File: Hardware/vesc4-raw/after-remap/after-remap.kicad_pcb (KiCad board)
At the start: 4 copper layers, 38.5 x 65 mm, 127 parts, among them K1 SERVO, P1 HALL/Encoder, P101 CANBUS, P2 SWD, P3 PWR_COMM, P4 IN+, P5 IN-, P6 MOTOR1, P7 MOTOR2, P9 MOTOR3, Q1 IPT007N06NATMA1, Q2 IPT007N06NATMA1, Q3 IPT007N06NATMA1, Q4 IPT007N06NATMA1, Q5 IPT007N06NATMA1, Q6 IPT007N06NATMA1, U1 STM32F40X_LQFP64, U2 TC2117, U3 DRV8302, U401 SN65HVD232, X1 MINI-USB-SHIELD-32005-201, X2 8MHz 10ppm

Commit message: changed phase 3
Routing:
- net /Power MOSFETS/Q5-s_Q6-d: track 166.9 -> 175.3 mm, vias 18 -> 20
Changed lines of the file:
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@@
-	)
-	(segment
-		(start 86.36 90.932)
-		(end 84.836 90.678)
-		(width 0.508)
-		(layer "F.Cu")
-		(net 69)
 	)
 	(segment
@@
 	)
 	(segment
+		(start 86.36 90.932)
+		(end 86.4742 90.932)
+		(width 1.27)
+		(layer "F.Cu")
+		(net 69)
+	)
+	(segment
 		(start 86.36 89.154)
 		(end 86.36 87.122)
@@
 		(end 85.725 87.24646)
 		(width 0.508)
+		(layer "F.Cu")
+		(net 69)
+	)
+	(segment
+		(start 87.7 90.7)
+		(end 87.468 90.932)
+		(width 1.27)
 		(layer "F.Cu")
 		(net 69)
@@
 	)
 	(segment
+		(start 85.8 90.932)
+		(end 84.582 90.932)
+		(width 1.27)
+		(layer "F.Cu")
+		(net 69)
+	)
+	(segment
+		(start 87.468 90.932)
+		(end 85.8 90.932)
+		(width 1.27)
+		(layer "F.Cu")
+		(net 69)
+	)
+	(segment
+		(start 87.9062 89.5)
+		(end 86.948527 88.542327)
+		(width 0.2032)
+		(layer "F.Cu")
+		(net 69)
+	)
+	(segment
+		(start 85.8 90.932)
+		(end 86.4742 90.932)
+		(width 1.27)
+		(layer "F.Cu")
+		(net 69)
+	)
+	(segment
+		(start 86.749702 88.542327)
+		(end 87.8441 89.636725)
+		(width 1.27)
+		(layer "F.Cu")
+		(net 69)
+	)
+	(segment
 		(start 104.267 104.233266)
 		(end 104.267 107.442)
@@
 	)
 	(segment
-		(start 86.36 90.932)
-		(end 84.582 90.932)
+		(start 86.749702 90.656498)
+		(end 86.749702 88.542327)
 		(width 1.27)
 		(layer "F.Cu")
@@
 	)
 	(segment
+		(start 86.749702 88.542327)
+		(end 87.8441 88.542327)
+		(width 1.27)
+		(layer "F.Cu")
+		(net 69)
+	)
+	(segment
+		(start 87.8441 89.636725)
+		(end 87.8441 90.442327)
+		(width 1.27)
+		(layer "F.Cu")
+		(net 69)
+	)
+	(segment
 		(start 85.979 87.24646)
 		(end 85.979 83.693)
@@
 	)
 	(segment
+		(start 86.948527 88.542327)
+		(end 86.749702 88.542327)
+		(width 0.2032)
+		(layer "F.Cu")
+		(net 69)
+	)
+	(segment
 		(start 105.15854 110.779958)
 		(end 104.14 109.761418)
@@
 		(net 69)
 	)
-	(via
-		(at 86.36 87.122)
-		(size 1.524)
-		(drill 0.762)
-		(layers "F.Cu" "B.Cu")
-		(net 69)
-	)
-	(via
-		(at 84.582 89.154)
-		(size 1.524)
-		(drill 0.762)
+	(segment
+		(start 86.4742 90.932)
+		(end 86.749702 90.656498)
+		(width 1.27)
+		(layer "F.Cu")
+		(net 69)
+	)
+	(via
+		(at 86.749702 88.542327)
+		(size 0.8)
+		(drill 0.5)
+		(layers "F.Cu" "B.Cu")
+		(net 69)
+	)
+	(via
+		(at 87.949702 88.542327)
+		(size 0.8)
+		(drill 0.5)
+		(layers "F.Cu" "B.Cu")
+		(net 69)
+	)
+	(via
+		(at 84.349702 90.442327)
+		(size 0.8)
+		(drill 0.5)
+		(layers "F.Cu" "B.Cu")
+		(net 69)
+	)
+	(via
+		(at 84.349702 88.542327)
+		(size 0.8)
+		(drill 0.5)
 		(layers "F.Cu" "B.Cu")
 		(net 69)
@@
 	)
 	(via
-		(at 82.804 90.932)
-		(size 1.524)
-		(drill 0.762)
-		(layers "F.Cu" "B.Cu")
-		(net 69)
-	)
-	(via
-		(at 82.804 87.122)
-		(size 1.524)
-		(drill 0.762)
-		(layers "F.Cu" "B.Cu")
-		(net 69)
-	)
-	(via
-		(at 82.804 89.154)
-		(size 1.524)
-		(drill 0.762)
-		(layers "F.Cu" "B.Cu")
-		(net 69)
-	)
-	(via
-		(at 81.026 89.154)
-		(size 1.524)
-		(drill 0.762)
+		(at 81.949702 88.542327)
+		(size 0.8)
+		(drill 0.5)
 		(layers "F.Cu" "B.Cu")
 		(net 69)
@@
 		(at 91.44 86.868)
 		(size 0.889)
+		(drill 0.5)
+		(layers "F.Cu" "B.Cu")
+		(net 69)
+	)
+	(via
+		(at 83.149702 88.542327)
+		(size 0.8)
+		(drill 0.5)
+		(layers "F.Cu" "B.Cu")
+		(net 69)
+	)
+	(via
+		(at 85.549702 88.542327)
+		(size 0.8)
 		(drill 0.5)
 		(layers "F.Cu" "B.Cu")
@@
 	)
 	(via
+		(at 80.749702 90.442327)
+		(size 0.8)
+		(drill 0.5)
+		(layers "F.Cu" "B.Cu")
+		(net 69)
+	)
+	(via
 		(at 104.5 104.000266)
 		(size 0.8)
 		(drill 0.5)
-		(layers "F.Cu" "B.Cu")
-		(net 69)
-	)
-	(via
-		(at 81.026 90.932)
-		(size 1.524)
-		(drill 0.762)
 		(layers "F.Cu" "B.Cu")
 		(net 69)
@@
 	)
 	(via
-		(at 86.36 90.932)
-		(size 1.524)
-		(drill 0.762)
+		(at 81.949702 90.442327)
+		(size 0.8)
+		(drill 0.5)
 		(layers "F.Cu" "B.Cu")
 		(net 69)
@@
 	)
 	(via
-		(at 84.582 87.122)
-		(size 1.524)
-		(drill 0.762)
-		(layers "F.Cu" "B.Cu")
-		(net 69)
-	)
-	(via
-		(at 81.026 87.122)
-		(size 1.524)
-		(drill 0.762)
-		(layers "F.Cu" "B.Cu")
-		(net 69)
-	)
-	(via
-		(at 86.36 89.154)
-		(size 1.524)
-		(drill 0.762)
-		(layers "F.Cu" "B.Cu")
-		(net 69)
-	)
-	(via
-		(at 84.582 90.932)
-		(size 1.524)
-		(drill 0.762)
+		(at 87.949702 90.442327)
+		(size 0.8)
+		(drill 0.5)
+		(layers "F.Cu" "B.Cu")
+		(net 69)
+	)
+	(via
+		(at 86.749702 90.442327)
+		(size 0.8)
+		(drill 0.5)
+		(layers "F.Cu" "B.Cu")
+		(net 69)
+	)
+	(via
+		(at 83.149702 90.442327)
+		(size 0.8)
+		(drill 0.5)
+		(layers "F.Cu" "B.Cu")
+		(net 69)
+	)
+	(via
+		(at 85.549702 90.442327)
+		(size 0.8)
+		(drill 0.5)
+		(layers "F.Cu" "B.Cu")
+		(net 69)
+	)
+	(via
+		(at 80.749702 88.542327)
+		(size 0.8)
+		(drill 0.5)
 		(layers "F.Cu" "B.Cu")
 		(net 69)
@@
 	)
 	(segment
-		(start 86.614 86.868)
-		(end 86.36 87.122)
-		(width 1.27)
-		(layer "In2.Cu")
-		(net 69)
-	)
-	(segment
 		(start 98.539266 104.000266)
 		(end 95.504 100.965)
@@
 	)
 	(segment
+		(start 88.424029 86.868)
+		(end 86.749702 88.542327)
+		(width 1.27)
+		(layer "In2.Cu")
+		(net 69)
+	)
+	(segment
 		(start 89.789 111.76)
 		(end 93.726 111.76)
@@
 	)
 	(segment
-		(start 91.44 86.868)
-		(end 86.614 86.868)
-		(width 1.27)
-		(layer "In2.Cu")
-		(net 69)
-	)
-	(segment
 		(start 90.932 100.965)
 		(end 88.392 103.505)
@@
 		(layer "In2.Cu")
 		(net 69)
+	)
+	(segment
+		(start 91.44 86.868)
+		(end 88.424029 86.868)
+		(width 1.27)
+		(layer "In2.Cu")
+		(net 69)

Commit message: change phase tengah
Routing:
- net /Power MOSFETS/Q3-s_Q4-d: track 145.0 -> 145.9 mm, vias 17 -> 19

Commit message: pindahin via untuk perbanyak contact
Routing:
- net /Power MOSFETS/Q3-s_Q4-d: track 145.9 -> 153.3 mm
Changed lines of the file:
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@@
 	(segment
 		(start 104.394 91.694)
-		(end 105.537509 92.837509)
+		(end 104.4 91.7)
 		(width 0.635)
 		(layer "In1.Cu")
@@
 	)
 	(segment
-		(start 105.537509 92.837509)
-		(end 105.537509 101.941532)
+		(start 104.4 93.4)
+		(end 105.537509 94.537509)
 		(width 0.635)
 		(layer "In1.Cu")
@@
 	)
 	(segment
-		(start 105.537509 101.941532)
+		(start 105.537509 94.537509)
 		(end 105.537509 102.507217)
 		(width 0.635)
@@
 	)
 	(segment
+		(start 104.4 91.7)
+		(end 104.4 93.4)
+		(width 0.635)
+		(layer "In1.Cu")
+		(net 17)
+	)
+	(segment
 		(start 102.9966 112.845202)
 		(end 102.596601 113.245201)
@@
 	)
 	(segment
-		(start 100.7441 88.68528)
-		(end 100.7441 90.58528)
+		(start 100.7441 90.58528)
+		(end 100.65138 90.678)
 		(width 1.27)
 		(layer "F.Cu")
@@
 	)
 	(segment
-		(start 99.0186 88.9)
-		(end 100.52938 88.9)
-		(width 1.27)
-		(layer "F.Cu")
-		(net 68)
-	)
-	(segment
 		(start 97.79 82.804)
 		(end 98.171 82.804)
@@
 	)
 	(segment
+		(start 100.52938 88.9)
+		(end 100.7441 88.68528)
+		(width 1.27)
+		(layer "F.Cu")
+		(net 68)
+	)
+	(segment
 		(start 102.489 108.839)
 		(end 102.489 105.41)
@@
 	)
 	(segment
-		(start 100.7441 90.58528)
-		(end 100.65138 90.678)
+		(start 98.4186 89.5)
+		(end 99.0186 88.9)
 		(width 1.27)
 		(layer "F.Cu")
@@
 	)
 	(segment
-		(start 100.52938 88.9)
-		(end 100.7441 88.68528)
+		(start 100.65138 90.678)
+		(end 100.32938 91)
 		(width 1.27)
 		(layer "F.Cu")
@@
 	)
 	(segment
+		(start 100.7441 88.68528)
+		(end 100.7441 90.58528)
+		(width 1.27)
+		(layer "F.Cu")
+		(net 68)
+	)
+	(segment
 		(start 102.489 104.5337)
 		(end 103.790707 103.231993)
@@
 	)
 	(segment
+		(start 100.32938 91)
+		(end 93.732 91)
+		(width 1.27)
+		(layer "F.Cu")
+		(net 68)
+	)
+	(segment
 		(start 95.758 90.678)
 		(end 97.79 90.678)
@@
 	)
 	(segment
-		(start 98.4186 89.5)
-		(end 99.0186 88.9)
-		(width 1.27)
-		(layer "F.Cu")
-		(net 68)
-	)
-	(segment
 		(start 95.758 90.678)
 		(end 95.758 88.9)
@@
 	)
 	(segment
+		(start 99.0186 88.9)
+		(end 100.52938 88.9)
+		(width 1.27)
+		(layer "F.Cu")
+		(net 68)
+	)
+	(segment
 		(start 102.730299 110.730027)
 		(end 102.730299 109.080299)
@@
 	)
 	(via
-		(at 96.033048 90.496332)
+		(at 96.033048 91.234337)
 		(size 0.8)
 		(drill 0.5)
@@
 	)
 	(via
-		(at 100.833048 88.596332)
+		(at 100.833048 87.72272)
 		(size 0.8)
 		(drill 0.5)
@@
 	)
 	(via
-		(at 96.033048 88.596332)
+		(at 96.033048 87.72272)
 		(size 0.8)
 		(drill 0.5)
@@
 	)
 	(via
-		(at 93.633048 88.596332)
+		(at 93.633048 87.72272)
 		(size 0.8)
 		(drill 0.5)
@@
 	)
 	(via
-		(at 94.833048 90.496332)
+		(at 94.833048 91.234337)
 		(size 0.8)
 		(drill 0.5)
@@
 	)
 	(via
-		(at 98.433048 90.496332)
+		(at 98.433048 91.234337)
 		(size 0.8)
 		(drill 0.5)
@@
 	)
 	(via
-		(at 99.633048 90.496332)
+		(at 99.633048 91.234337)
 		(size 0.8)
 		(drill 0.5)
@@
 	)
 	(via
-		(at 93.633048 90.496332)
+		(at 93.633048 91.234337)
 		(size 0.8)
 		(drill 0.5)
@@
 	)
 	(via
-		(at 94.833048 88.596332)
+		(at 94.833048 87.72272)
 		(size 0.8)
 		(drill 0.5)
@@
 	)
 	(via
-		(at 97.233048 88.596332)
+		(at 97.233048 87.72272)
 		(size 0.8)
 		(drill 0.5)
@@
 	)
 	(via
-		(at 97.233048 90.496332)
+		(at 97.233048 91.234337)
 		(size 0.8)
 		(drill 0.5)
@@
 	)
 	(via
-		(at 98.433048 88.596332)
+		(at 98.433048 87.72272)
 		(size 0.8)
 		(drill 0.5)
@@
 	)
 	(via
-		(at 99.633048 88.596332)
+		(at 99.633048 87.72272)
 		(size 0.8)
 		(drill 0.5)
@@
 	)
 	(via
-		(at 100.833048 90.496332)
+		(at 100.833048 91.234337)
 		(size 0.8)
 		(drill 0.5)
@@
 	)
 	(segment
+		(start 102.010328 88.9)
+		(end 103.378 88.9)
+		(width 0.635)
+		(layer "In1.Cu")
+		(net 68)
+	)
+	(segment
 		(start 97.396311 111.391689)
 		(end 104.406689 111.391689)
@@
 	)
 	(segment
+		(start 107.1 102.691825)
+		(end 106.159825 103.632)
+		(width 0.635)
+		(layer "In1.Cu")
+		(net 68)
+	)
+	(segment
 		(start 104.406689 111.391689)
 		(end 106.172 113.157)
@@
 	)
 	(segment
-		(start 103.378 88.9)
-		(end 107.1 92.622)
-		(width 0.635)
+		(start 105.994139 104.031999)
+		(end 105.59414 103.632)
+		(width 0.254)
 		(layer "In1.Cu")
 		(net 68)
 	)
 	(segment
-		(start 107.1 102.691825)
-		(end 106.159825 103.632)
-		(width 0.635)
+		(start 91.2 123.6)
+		(end 90.800001 123.200001)
+		(width 0.254)
 		(layer "In1.Cu")
 		(net 68)
 	)
 	(segment
-		(start 105.994139 104.031999)
-		(end 105.59414 103.632)
-		(width 0.254)
+		(start 105.5 93.1)
+		(end 107.1 94.7)
+		(width 0.635)
 		(layer "In1.Cu")
 		(net 68)
 	)
 	(segment
-		(start 91.2 123.6)
-		(end 90.800001 123.200001)
-		(width 0.254)
+		(start 99.633048 87.72272)
+		(end 100.833048 87.72272)
+		(width 0.635)
 		(layer "In1.Cu")
 		(net 68)
@@
 	)
 	(segment
-		(start 99.633048 88.596332)
-		(end 99.936716 88.9)
-		(width 0.635)
-		(layer "In1.Cu")
-		(net 68)
-	)
-	(segment
 		(start 106.159825 103.632)
 		(end 105.41 103.632)
@@
 	)
 	(segment
-		(start 107.1 92.622)
-		(end 107.1 102.691825)
+		(start 100.833048 87.72272)
+		(end 102.010328 88.9)
 		(width 0.635)
 		(layer "In1.Cu")
@@
 	)
 	(segment
-		(start 99.936716 88.9)
-		(end 103.378 88.9)
+		(start 105.5 91.022)
+		(end 105.5 93.1)
 		(width 0.635)
 		(layer "In1.Cu")
@@
 	)
 	(segment
+		(start 107.1 94.7)
+		(end 107.1 102.691825)
+		(width 0.635)
+		(layer "In1.Cu")
+		(net 68)
+	)
+	(segment
+		(start 103.378 88.9)
+		(end 105.5 91.022)
+		(width 0.635)
+		(layer "In1.Cu")
+		(net 68)
+	)
+	(segment
 		(start 83.312 85.598)
 		(end 83.312 87.122)
@@
 	)
 	(via
-		(at 86.749702 88.542327)
+		(at 86.730095 87.72272)
 		(size 0.8)
 		(drill 0.5)
@@
 	)
 	(via
-		(at 87.949702 88.542327)
+		(at 87.930095 87.72272)
 		(size 0.8)
 		(drill 0.5)
@@
 	)
 	(via
-		(at 84.349702 90.442327)
+		(at 84.341138 91.234337)
 		(size 0.8)
 		(drill 0.5)
@@
 	)
 	(via
-		(at 84.349702 88.542327)
+		(at 84.330095 87.72272)
 		(size 0.8)
 		(drill 0.5)
@@
 	)
 	(via
-		(at 81.949702 88.542327)
+		(at 81.930095 87.72272)
 		(size 0.8)
 		(drill 0.5)
@@
 	)
 	(via
-		(at 83.149702 88.542327)
+		(at 83.130095 87.72272)
 		(size 0.8)
 		(drill 0.5)
@@
 	)
 	(via
-		(at 85.549702 88.542327)
+		(at 85.530095 87.72272)
 		(size 0.8)
 		(drill 0.5)
@@
 	)
 	(via
-		(at 80.749702 90.442327)
+		(at 80.741138 91.234337)
 		(size 0.8)
 		(drill 0.5)
@@
 	)
 	(via
-		(at 81.949702 90.442327)
+		(at 81.941138 91.234337)
 		(size 0.8)
 		(drill 0.5)
@@
 	)
 	(via
-		(at 87.949702 90.442327)
+		(at 87.941138 91.234337)
 		(size 0.8)
 		(drill 0.5)
@@
 	)
 	(via
-		(at 86.749702 90.442327)
+		(at 86.741138 91.234337)
 		(size 0.8)
 		(drill 0.5)
@@
 	)
 	(via
-		(at 83.149702 90.442327)
+		(at 83.141138 91.234337)
 		(size 0.8)
 		(drill 0.5)
@@
 	)
 	(via
-		(at 85.549702 90.442327)
+		(at 85.541138 91.234337)
 		(size 0.8)
 		(drill 0.5)
@@
 	)
 	(via
-		(at 80.749702 88.542327)
+		(at 80.730095 87.72272)
 		(size 0.8)
 		(drill 0.5)

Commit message: done changed via numpuk
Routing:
- net /Power MOSFETS/Q1-s_Q2-d: track 150.9 -> 159.1 mm, vias 17 -> 19

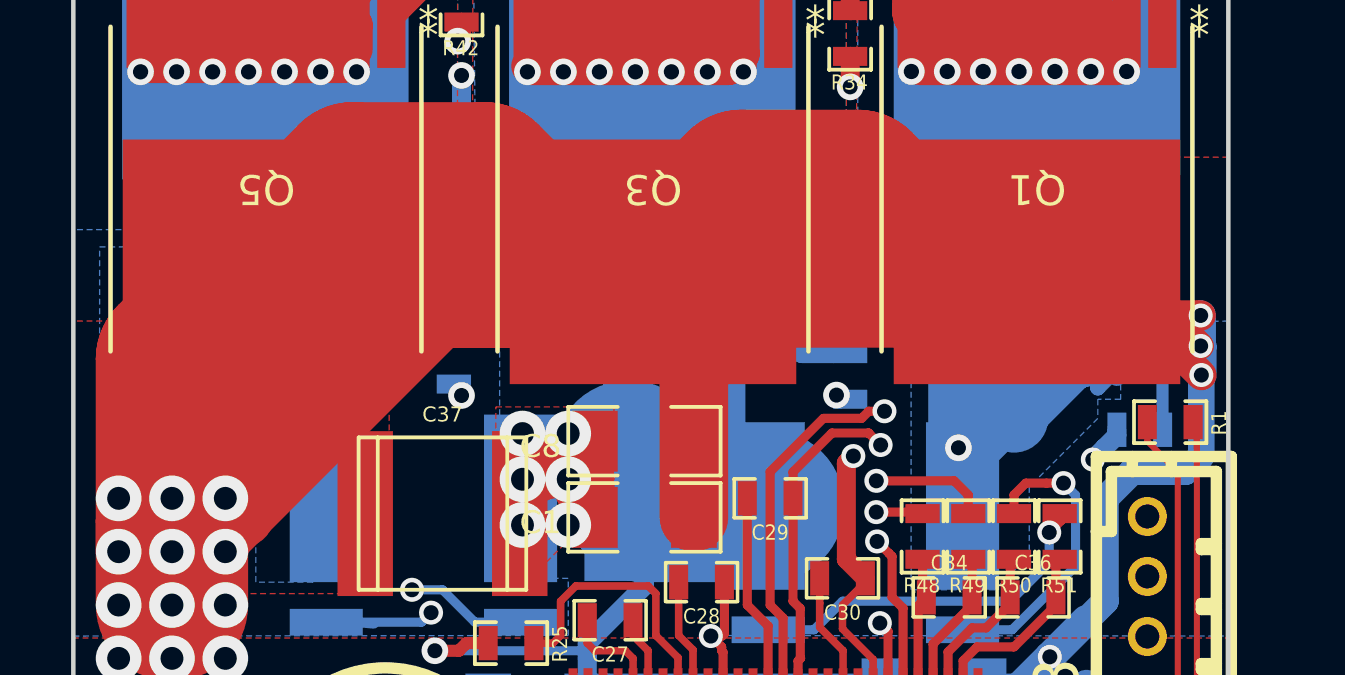
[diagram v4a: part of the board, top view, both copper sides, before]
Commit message: added thermal vias on front mosfets
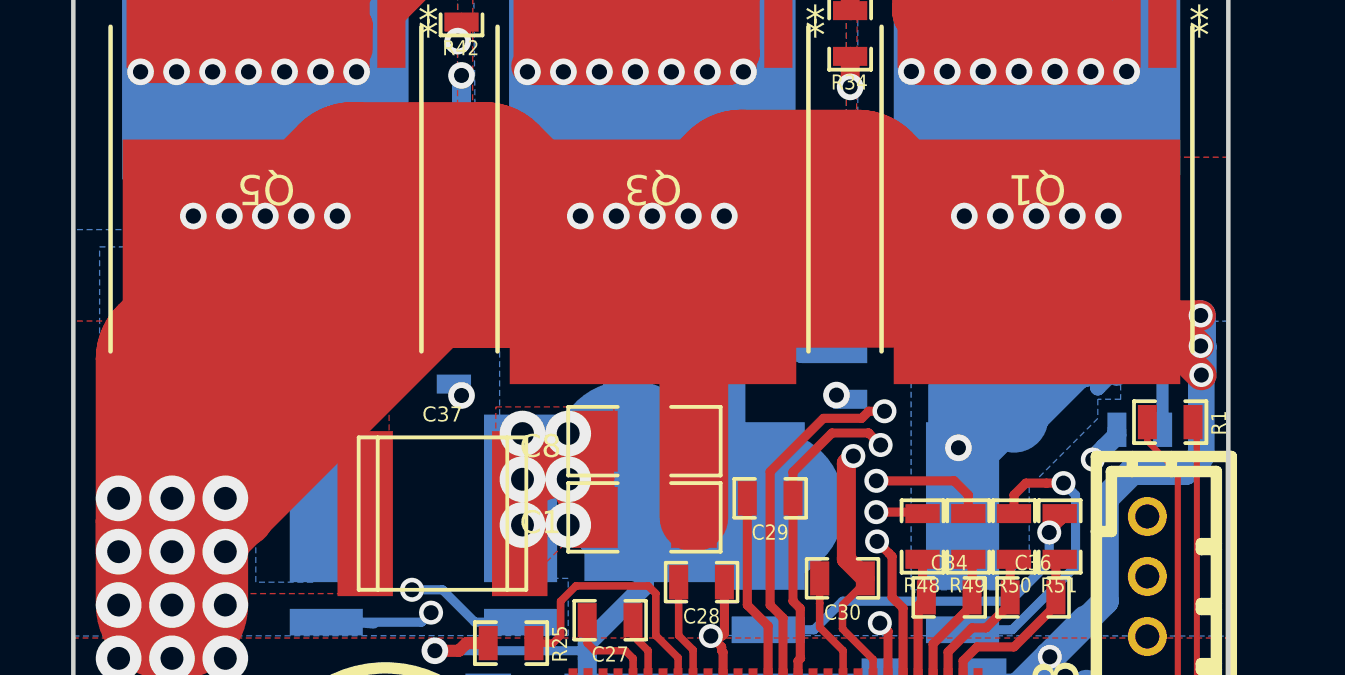
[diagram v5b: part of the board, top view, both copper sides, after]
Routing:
- net /Power MOSFETS/Q2-g: track 17.3 -> 18.6 mm
- net V_SUPPLY: vias 20 -> 35
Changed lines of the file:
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@@
 	)
 	(via
+		(at 109.4 96)
+		(size 0.889)
+		(drill 0.508)
+		(layers "F.Cu" "B.Cu")
+		(net 9)
+	)
+	(via
 		(at 111.049589 110.692411)
 		(size 0.8)
@@
 	)
 	(via
+		(at 100.2 96)
+		(size 0.889)
+		(drill 0.508)
+		(layers "F.Cu" "B.Cu")
+		(net 9)
+	)
+	(via
+		(at 97.8 96)
+		(size 0.889)
+		(drill 0.508)
+		(layers "F.Cu" "B.Cu")
+		(net 9)
+	)
+	(via
 		(at 93.98 113.411)
 		(size 0.8)
@@
 	)
 	(via
+		(at 84.9 96)
+		(size 0.889)
+		(drill 0.508)
+		(layers "F.Cu" "B.Cu")
+		(net 9)
+	)
+	(via
 		(at 81.788 108.966)
 		(size 1.524)
@@
 	)
 	(via
+		(at 113 96)
+		(size 0.889)
+		(drill 0.508)
+		(layers "F.Cu" "B.Cu")
+		(net 9)
+	)
+	(via
 		(at 116.1 101.3)
 		(size 0.8)
@@
 	)
 	(via
+		(at 110.6 96)
+		(size 0.889)
+		(drill 0.508)
+		(layers "F.Cu" "B.Cu")
+		(net 9)
+	)
+	(via
 		(at 81.788 105.41)
 		(size 1.524)
@@
 	)
 	(via
+		(at 108.2 96)
+		(size 0.889)
+		(drill 0.508)
+		(layers "F.Cu" "B.Cu")
+		(net 9)
+	)
+	(via
 		(at 83.9 125.3)
 		(size 0.8)
@@
 	)
 	(via
+		(at 82.5 96)
+		(size 0.889)
+		(drill 0.508)
+		(layers "F.Cu" "B.Cu")
+		(net 9)
+	)
+	(via
+		(at 95.4 96)
+		(size 0.889)
+		(drill 0.508)
+		(layers "F.Cu" "B.Cu")
+		(net 9)
+	)
+	(via
+		(at 87.3 96)
+		(size 0.889)
+		(drill 0.508)
+		(layers "F.Cu" "B.Cu")
+		(net 9)
+	)
+	(via
+		(at 83.7 96)
+		(size 0.889)
+		(drill 0.508)
+		(layers "F.Cu" "B.Cu")
+		(net 9)
+	)
+	(via
+		(at 86.1 96)
+		(size 0.889)
+		(drill 0.508)
+		(layers "F.Cu" "B.Cu")
+		(net 9)
+	)
+	(via
+		(at 96.6 96)
+		(size 0.889)
+		(drill 0.508)
+		(layers "F.Cu" "B.Cu")
+		(net 9)
+	)
+	(via
 		(at 83.566 110.744)
 		(size 1.524)
@@
 	)
 	(via
+		(at 99 96)
+		(size 0.889)
+		(drill 0.508)
+		(layers "F.Cu" "B.Cu")
+		(net 9)
+	)
+	(via
+		(at 111.8 96)
+		(size 0.889)
+		(drill 0.508)
+		(layers "F.Cu" "B.Cu")
+		(net 9)
+	)
+	(via
 		(at 83.566 107.188)
 		(size 1.524)
@@
 	(segment
 		(start 104.394 95.377)
-		(end 113.3423 95.377)
+		(end 104.871 94.9)
 		(width 0.2032)
 		(layer "B.Cu")
@@
 	)
 	(segment
-		(start 113.3423 95.377)
-		(end 114.8 96.8347)
+		(start 114.808 103.124)
+		(end 114.808 98.608)
+		(width 0.4064)
+		(layer "B.Cu")
+		(net 87)
+	)
+	(segment
+		(start 105.5939 94.9029)
+		(end 114.4029 94.9029)
 		(width 0.2032)
 		(layer "B.Cu")
@@
 	)
 	(segment
-		(start 114.808 103.124)
-		(end 114.808 98.608)
-		(width 0.4064)
+		(start 104.871 94.9)
+		(end 105.5939 94.9)
+		(width 0.2032)
 		(layer "B.Cu")
 		(net 87)
 	)
 	(segment
-		(start 114.8 96.8347)
+		(start 114.808 98.608)
 		(end 114.8 98.6)
 		(width 0.2032)
@@
 	)
 	(segment
-		(start 114.808 98.608)
+		(start 105.5939 94.9)
+		(end 105.5939 94.9029)
+		(width 0.2032)
+		(layer "B.Cu")
+		(net 87)
+	)
+	(segment
+		(start 114.8 95.3)
 		(end 114.8 98.6)
 		(width 0.2032)
@@
 	)
 	(segment
+		(start 114.4029 94.9029)
+		(end 114.8 95.3)
+		(width 0.2032)
+		(layer "B.Cu")
+		(net 87)
+	)
+	(segment
 		(start 103.9 87.3)
 		(end 104.394 87.794)
@@
 	)
 	(segment
-		(start 91.186 96.774)
-		(end 90.17 95.758)
-		(width 0.2032)
+		(start 89.242 95.758)
+		(end 87.376 97.624)
+		(width 0.635)
 		(layer "B.Cu")
 		(net 96)
 	)
 	(segment
-		(start 90.17 95.758)
-		(end 88.519 95.758)
-		(width 0.635)
+		(start 91.186 96.774)
+		(end 90.17 95.758)
+		(width 0.2032)
 		(layer "B.Cu")
 		(net 96)
 	)
 	(segment
-		(start 91.186 97.282)
-		(end 91.186 96.774)
-		(width 0.2032)
+		(start 87.376 97.624)
+		(end 87.376 104.9655)
+		(width 0.635)
 		(layer "B.Cu")
 		(net 96)
@@
 	)
 	(segment
-		(start 88.519 95.758)
-		(end 87.376 96.901)
-		(width 0.635)
+		(start 91.186 97.282)
+		(end 91.186 96.774)
+		(width 0.2032)
 		(layer "B.Cu")
 		(net 96)
 	)
 	(segment
-		(start 87.376 96.901)
-		(end 87.376 104.9655)
+		(start 90.17 95.758)
+		(end 89.242 95.758)
 		(width 0.635)
 		(layer "B.Cu")

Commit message: ganti schematic
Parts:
- added USB1: ~, EasyEDA_Lib:MICRO-USB-SMD_HX-USB-MICRO-XNJ-JB, F.Cu at (75.7, 127.6)
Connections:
- R103 pad 2: Net-(R103-Pad2) -> Net-(USB1-D-)
- R104 pad 2: Net-(R104-Pad2) -> Net-(USB1-D+)
- R6 pad 1: Net-(R6-Pad1) -> Net-(USB1-VCC)

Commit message: sebelum ganti komponen
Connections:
- USB1 pad 1: Net-(USB1-VCC) -> Net-(D6-A)
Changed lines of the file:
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@@
 	(net 118 "Net-(USB1-D+)")
 	(net 119 "unconnected-(USB1-ID-Pad4)")
+	(net 120 "Net-(D6-A)")
 	(footprint "VESC4-legacy:1pin"
 		(layer "F.Cu")
@@
 			(size 0.4 1.6)
 			(layers "F.Cu" "F.Mask" "F.Paste")
-			(net 116 "Net-(USB1-VCC)")
+			(net 120 "Net-(D6-A)")
 			(pinfunction "VCC")
 			(pintype "input")

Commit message: checkpoint sebelum ngetrace usb
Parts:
- removed USB1: ~, EasyEDA_Lib:MICRO-USB-SMD_HX-USB-MICRO-XNJ-JB
- removed X1: MINI-USB-SHIELD-32005-201, CRF1:USB-UX60R-MB-5ST
- added D4: ~, EasyEDA_Lib:SMA_L4.2-W2.6-LS5.1-RD, F.Cu at (67.8, 107.8)
- added D6: ~, EasyEDA_Lib:SMA_L4.2-W2.6-LS5.1-RD, F.Cu at (67.9, 111.9)
- added U4: ~, EasyEDA_Lib:MICRO-USB-SMD_MICROUSB-5P-M, F.Cu at (80.2, 128.0)
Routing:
- net GND: track 399.7 -> 387.7 mm
- net Net-(R6-Pad1): track 5.50 -> 0.00 mm, vias 1 -> 0
- net Net-(USB1-VCC): track 0.00 -> 4.72 mm, vias 0 -> 1
- net Net-(U4-D+): track 0.00 -> 4.28 mm
- net Net-(R104-Pad2): track 4.28 -> 0.00 mm
- net Net-(U4-D-): track 0.00 -> 3.97 mm
- net Net-(R103-Pad2): track 3.97 -> 0.00 mm
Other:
- board size 38.5 x 65 mm -> 40.3 x 65 mm
